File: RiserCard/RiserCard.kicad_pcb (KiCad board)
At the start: 2 copper layers, 150 x 76 mm, 0 parts

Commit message: Mid-work commit. Add README
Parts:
- added U1: 86094327313755ELF, Kicad_Library:DIN41612_C2_2x16_Male_Horizontal_THT, F.Cu at (45.3, 97.0)
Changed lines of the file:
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@@
     (tracks 0)
     (zones 0)
-    (modules 0)
-    (nets 1)
+    (modules 1)
+    (nets 4)
   )
   (page A4)
@@
   )
   (net 0 "")
+  (net 1 +5V)
+  (net 2 +3V3)
+  (net 3 GND)
   (net_class Default "This is the default net class."
     (clearance 0.2)
@@
     (uvia_dia 0.3)
     (uvia_drill 0.1)
+    (add_net +3V3)
+    (add_net +5V)
+    (add_net /EN_ICSP_A)
+    (add_net /EN_ICSP_B)
+    (add_net /EN_JTAG_A)
+    (add_net /EN_JTAG_B)
+    (add_net /EN_PWR_A)
+    (add_net /EN_PWR_B)
+    (add_net /PGEC)
+    (add_net /PGED)
+    (add_net /SPARE_A)
+    (add_net /SPARE_B)
+    (add_net /TARGET_RX)
+    (add_net /TARGET_TX)
+    (add_net /TCK)
+    (add_net /TDI)
+    (add_net /TDO)
+    (add_net /TMS)
+    (add_net /~MCLR)
+    (add_net GND)
+    (add_net "Net-(U1-Pada10)")
+    (add_net "Net-(U1-Pada11)")
+    (add_net "Net-(U1-Pada12)")
+    (add_net "Net-(U1-Pada13)")
+    (add_net "Net-(U1-Pada5)")
+    (add_net "Net-(U1-Pada6)")
+    (add_net "Net-(U1-Pada7)")
+    (add_net "Net-(U1-Pada8)")
+    (add_net "Net-(U1-Pada9)")
+  )
+  (module Kicad_Library:DIN41612_C2_2x16_Male_Horizontal_THT (layer F.Cu)
+    (at 45.3 97.05 90)
+    (descr "DIN41612 connector, type C/2, Horizontal, 3 rows 16 pins wide, https://www.erni-x-press.com/de/downloads/kataloge/englische_kataloge/erni-din41612-iec60603-2-e.pdf")
+    (tags "DIN 41612 IEC 60603 C/2")
+    (fp_text reference U1 (at -5.08 1 90) (layer F.SilkS)
+      (effects (font (size 1 1) (thickness 0.15)))
+    )
+    (fp_text value 86094327313755ELF (at 19.05 7.62 90) (layer F.Fab)
+      (effects (font (size 1 1) (thickness 0.15)))
+    )
+    (fp_text user %R (at 19.05 -2.54 90) (layer F.Fab)
+      (effects (font (size 1 1) (thickness 0.15)))
+    )
+    (fp_text user "Board edge" (at 19.05 -7.3 90) (layer Cmts.User)
+      (effects (font (size 0.7 0.7) (thickness 0.1)))
+    )
+    (fp_line (start 19.05 -5.4) (end 19.05 -6.7) (layer Cmts.User) (width 0.1))
+    (fp_line (start 19.05 -5.4) (end 19.25 -5.9) (layer Cmts.User) (width 0.1))
+    (fp_line (start 18.85 -5.9) (end 19.05 -5.4) (layer Cmts.User) (width 0.1))
+    (fp_line (start -7.9 -5.3) (end 46 -5.3) (layer Dwgs.User) (width 0.08))
+    (fp_line (start 46.5 -13.23) (end -8.39 -13.23) (layer F.CrtYd) (width 0.05))
+    (fp_line (start 46.5 0.5) (end 46.5 -13.23) (layer F.CrtYd) (width 0.05))
+    (fp_line (start 39.38 0.5) (end 46.5 0.5) (layer F.CrtYd) (width 0.05))
+    (fp_line (start 39.38 6.36) (end 39.38 0.5) (layer F.CrtYd) (width 0.05))
+    (fp_line (start -1.27 6.36) (end 39.38 6.36) (layer F.CrtYd) (width 0.05))
+    (fp_line (start -1.27 0.5) (end -1.27 6.36) (layer F.CrtYd) (width 0.05))
+    (fp_line (start -8.39 0.5) (end -1.27 0.5) (layer F.CrtYd) (width 0.05))
+    (fp_line (start -8.39 -13.23) (end -8.39 0.5) (layer F.CrtYd) (width 0.05))
+    (fp_line (start 0.5 -1.9) (end 0 -1.2) (layer F.Fab) (width 0.1))
+    (fp_line (start -0.5 -1.9) (end 0.5 -1.9) (layer F.Fab) (width 0.1))
+    (fp_line (start 0 -1.2) (end -0.5 -1.9) (layer F.Fab) (width 0.1))
+    (fp_line (start -1.695 0.3) (end -1.095 0) (layer F.SilkS) (width 0.12))
+    (fp_line (start -1.695 -0.3) (end -1.695 0.3) (layer F.SilkS) (width 0.12))
+    (fp_line (start -1.095 0) (end -1.695 -0.3) (layer F.SilkS) (width 0.12))
+    (fp_line (start 38.97 -0.74) (end 40.74 -0.74) (layer F.SilkS) (width 0.12))
+    (fp_line (start 36.43 -0.74) (end 37.231 -0.74) (layer F.SilkS) (width 0.12))
+    (fp_line (start 33.89 -0.74) (end 34.691 -0.74) (layer F.SilkS) (width 0.12))
+    (fp_line (start 31.35 -0.74) (end 32.151 -0.74) (layer F.SilkS) (width 0.12))
+    (fp_line (start 28.81 -0.74) (end 29.611 -0.74) (layer F.SilkS) (width 0.12))
+    (fp_line (start 26.27 -0.74) (end 27.071 -0.74) (layer F.SilkS) (width 0.12))
+    (fp_line (start 23.73 -0.74) (end 24.531 -0.74) (layer F.SilkS) (width 0.12))
+    (fp_line (start 21.19 -0.74) (end 21.991 -0.74) (layer F.SilkS) (width 0.12))
+    (fp_line (start 18.65 -0.74) (end 19.451 -0.74) (layer F.SilkS) (width 0.12))
+    (fp_line (start 16.11 -0.74) (end 16.911 -0.74) (layer F.SilkS) (width 0.12))
+    (fp_line (start 13.57 -0.74) (end 14.371 -0.74) (layer F.SilkS) (width 0.12))
+    (fp_line (start 11.03 -0.74) (end 11.831 -0.74) (layer F.SilkS) (width 0.12))
+    (fp_line (start 8.49 -0.74) (end 9.291 -0.74) (layer F.SilkS) (width 0.12))
+    (fp_line (start 5.95 -0.74) (end 6.751 -0.74) (layer F.SilkS) (width 0.12))
+    (fp_line (start 3.41 -0.74) (end 4.211 -0.74) (layer F.SilkS) (width 0.12))
+    (fp_line (start 1.095 -0.74) (end 1.671 -0.74) (layer F.SilkS) (width 0.12))
+    (fp_line (start -2.64 -0.74) (end -1.095 -0.74) (layer F.SilkS) (width 0.12))
+    (fp_line (start 40.74 0.26) (end 40.74 -0.74) (layer F.SilkS) (width 0.12))
+    (fp_line (start 46.26 0.26) (end 40.74 0.26) (layer F.SilkS) (width 0.12))
+    (fp_line (start 46.26 -5.3) (end 46.26 0.26) (layer F.SilkS) (width 0.12))
+    (fp_line (start -2.64 0.26) (end -2.64 -0.74) (layer F.SilkS) (width 0.12))
+    (fp_line (start -8.16 0.26) (end -2.64 0.26) (layer F.SilkS) (width 0.12))
+    (fp_line (start -8.16 -5.3) (end -8.16 0.26) (layer F.SilkS) (width 0.12))
+    (fp_line (start 42.55 -12.74) (end -4.45 -12.74) (layer F.Fab) (width 0.1))
+    (fp_line (start 42.55 -6.74) (end 42.55 -12.74) (layer F.Fab) (width 0.1))
+    (fp_line (start 46 -6.74) (end 42.55 -6.74) (layer F.Fab) (width 0.1))
+    (fp_line (start 46 0) (end 46 -6.74) (layer F.Fab) (width 0.1))
+    (fp_line (start 41 0) (end 46 0) (layer F.Fab) (width 0.1))
+    (fp_line (start 41 -1) (end 41 0) (layer F.Fab) (width 0.1))
+    (fp_line (start -2.9 -1) (end 41 -1) (layer F.Fab) (width 0.1))
+    (fp_line (start -2.9 0) (end -2.9 -1) (layer F.Fab) (width 0.1))
+    (fp_line (start -7.9 0) (end -2.9 0) (layer F.Fab) (width 0.1))
+    (fp_line (start -7.9 -6.74) (end -7.9 0) (layer F.Fab) (width 0.1))
+    (fp_line (start -4.45 -6.74) (end -7.9 -6.74) (layer F.Fab) (width 0.1))
+    (fp_line (start -4.45 -12.74) (end -4.45 -6.74) (layer F.Fab) (width 0.1))
+    (pad "" np_thru_hole circle (at -5.08 -2.54 90) (size 2.85 2.85) (drill 2.85) (layers *.Cu *.Mask))
+    (pad "" np_thru_hole circle (at 43.18 -2.54 90) (size 2.85 2.85) (drill 2.85) (layers *.Cu *.Mask))
+    (pad a1 thru_hole roundrect (at 0 0 90) (size 1.55 1.55) (drill 1) (layers *.Cu *.Mask) (roundrect_rratio 0.16129))
+    (pad a2 thru_hole circle (at 2.54 0 90) (size 1.55 1.55) (drill 1) (layers *.Cu *.Mask))
+    (pad a3 thru_hole circle (at 5.08 0 90) (size 1.55 1.55) (drill 1) (layers *.Cu *.Mask))
+    (pad a4 thru_hole circle (at 7.62 0 90) (size 1.55 1.55) (drill 1) (layers *.Cu *.Mask))
+    (pad a5 thru_hole circle (at 10.16 0 90) (size 1.55 1.55) (drill 1) (layers *.Cu *.Mask))
+    (pad a6 thru_hole circle (at 12.7 0 90) (size 1.55 1.55) (drill 1) (layers *.Cu *.Mask))
+    (pad a7 thru_hole circle (at 15.24 0 90) (size 1.55 1.55) (drill 1) (layers *.Cu *.Mask))
+    (pad a8 thru_hole circle (at 17.78 0 90) (size 1.55 1.55) (drill 1) (layers *.Cu *.Mask))
+    (pad a9 thru_hole circle (at 20.32 0 90) (size 1.55 1.55) (drill 1) (layers *.Cu *.Mask))
+    (pad a10 thru_hole circle (at 22.86 0 90) (size 1.55 1.55) (drill 1) (layers *.Cu *.Mask))
+    (pad a11 thru_hole circle (at 25.4 0 90) (size 1.55 1.55) (drill 1) (layers *.Cu *.Mask))
+    (pad a12 thru_hole circle (at 27.94 0 90) (size 1.55 1.55) (drill 1) (layers *.Cu *.Mask))
+    (pad a13 thru_hole circle (at 30.48 0 90) (size 1.55 1.55) (drill 1) (layers *.Cu *.Mask))
+    (pad a14 thru_hole circle (at 33.02 0 90) (size 1.55 1.55) (drill 1) (layers *.Cu *.Mask)
+      (net 1 +5V))
+    (pad a15 thru_hole circle (at 35.56 0 90) (size 1.55 1.55) (drill 1) (layers *.Cu *.Mask)
+      (net 2 +3V3))
+    (pad a16 thru_hole circle (at 38.1 0 90) (size 1.55 1.55) (drill 1) (layers *.Cu *.Mask)
+      (net 3 GND))
+    (pad c1 thru_hole circle (at 0 5.08 90) (size 1.55 1.55) (drill 1) (layers *.Cu *.Mask))
+    (pad c2 thru_hole circle (at 2.54 5.08 90) (size 1.55 1.55) (drill 1) (layers *.Cu *.Mask))
+    (pad c3 thru_hole circle (at 5.08 5.08 90) (size 1.55 1.55) (drill 1) (layers *.Cu *.Mask))
+    (pad c4 thru_hole circle (at 7.62 5.08 90) (size 1.55 1.55) (drill 1) (layers *.Cu *.Mask))
+    (pad c5 thru_hole circle (at 10.16 5.08 90) (size 1.55 1.55) (drill 1) (layers *.Cu *.Mask))
+    (pad c6 thru_hole circle (at 12.7 5.08 90) (size 1.55 1.55) (drill 1) (layers *.Cu *.Mask))
+    (pad c7 thru_hole circle (at 15.24 5.08 90) (size 1.55 1.55) (drill 1) (layers *.Cu *.Mask))
+    (pad c8 thru_hole circle (at 17.78 5.08 90) (size 1.55 1.55) (drill 1) (layers *.Cu *.Mask))
+    (pad c9 thru_hole circle (at 20.32 5.08 90) (size 1.55 1.55) (drill 1) (layers *.Cu *.Mask))
+    (pad c10 thru_hole circle (at 22.86 5.08 90) (size 1.55 1.55) (drill 1) (layers *.Cu *.Mask))
+    (pad c11 thru_hole circle (at 25.4 5.08 90) (size 1.55 1.55) (drill 1) (layers *.Cu *.Mask))
+    (pad c12 thru_hole circle (at 27.94 5.08 90) (size 1.55 1.55) (drill 1) (layers *.Cu *.Mask))
+    (pad c13 thru_hole circle (at 30.48 5.08 90) (size 1.55 1.55) (drill 1) (layers *.Cu *.Mask))
+    (pad c14 thru_hole circle (at 33.02 5.08 90) (size 1.55 1.55) (drill 1) (layers *.Cu *.Mask)
+      (net 1 +5V))
+    (pad c15 thru_hole circle (at 35.56 5.08 90) (size 1.55 1.55) (drill 1) (layers *.Cu *.Mask)
+      (net 2 +3V3))
+    (pad c16 thru_hole circle (at 38.1 5.08 90) (size 1.55 1.55) (drill 1) (layers *.Cu *.Mask)
+      (net 3 GND))
+    (model ${KICUSTOM3DMOD}/86094327313755ELF.stp
+      (offset (xyz 43.45 15 10.8))
+      (scale (xyz 1 1 1))
+      (rotate (xyz 0 0 180))
+    )
   )
   (gr_line (start 190 40) (end 40 40) (layer Edge.Cuts) (width 0.05))

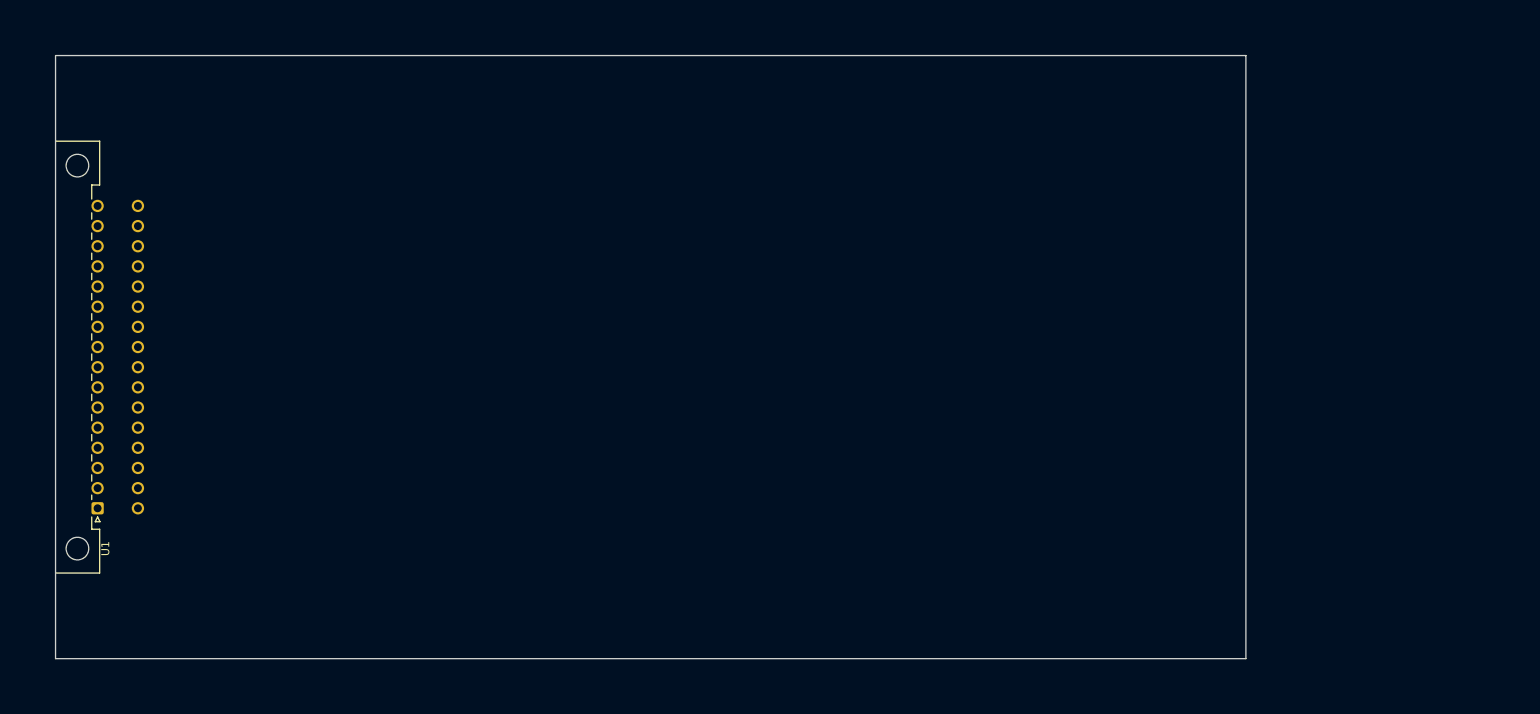
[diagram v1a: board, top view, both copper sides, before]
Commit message: mid-work commit, preparing the riser card
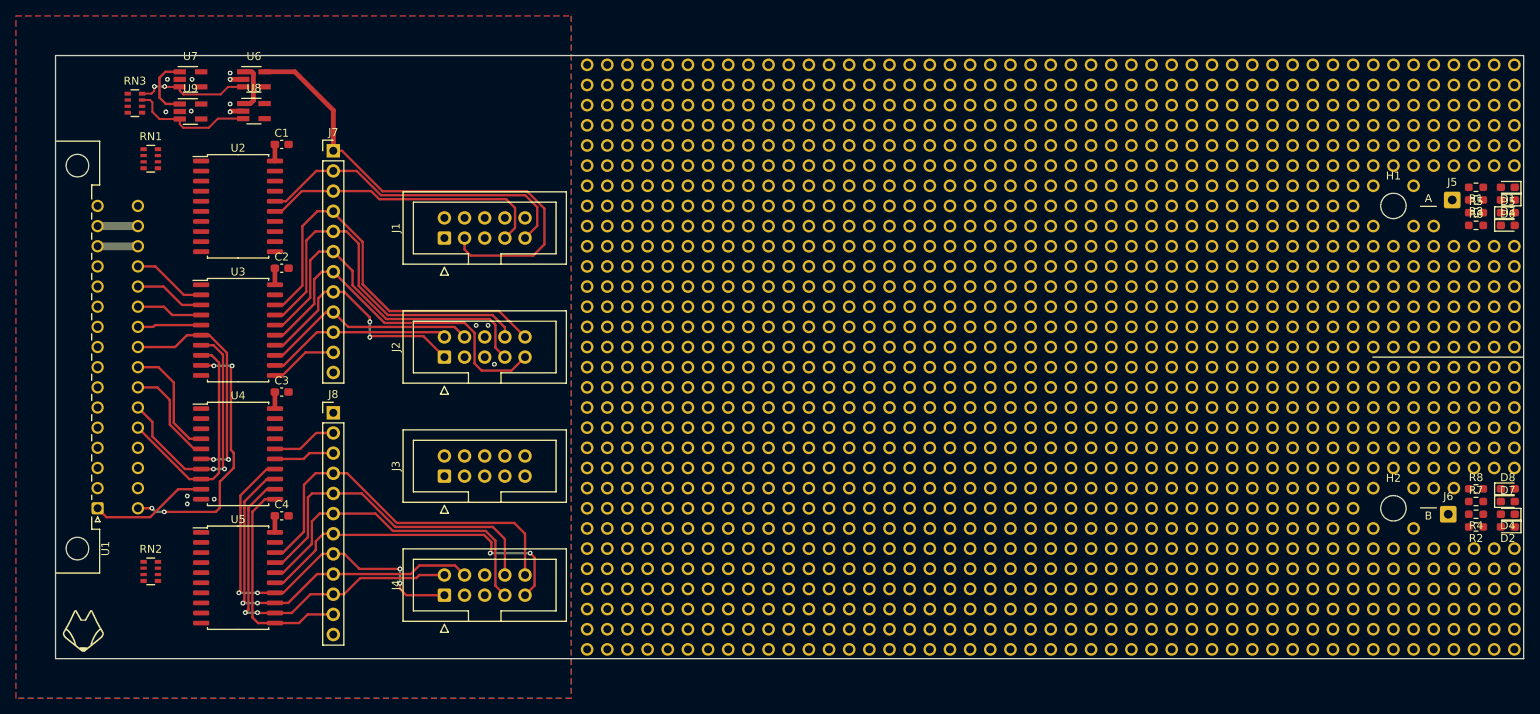
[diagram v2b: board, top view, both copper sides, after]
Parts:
- added C1: 100nF, Capacitor_SMD:C_0603_1608Metric_Pad1.08x0.95mm_HandSolder, F.Cu at (68.5, 51.2)
- added C2: 100nF, Capacitor_SMD:C_0603_1608Metric_Pad1.08x0.95mm_HandSolder, F.Cu at (68.5, 66.8)
- added C3: 100nF, Capacitor_SMD:C_0603_1608Metric_Pad1.08x0.95mm_HandSolder, F.Cu at (68.5, 82.4)
- added C4: 100nF, Capacitor_SMD:C_0603_1608Metric_Pad1.08x0.95mm_HandSolder, F.Cu at (68.5, 98.0)
- added D1: LED, LED_SMD:LED_0603_1608Metric_Pad1.05x0.95mm_HandSolder, F.Cu at (223.0, 56.6)
- added D2: LED, LED_SMD:LED_0603_1608Metric_Pad1.05x0.95mm_HandSolder, F.Cu at (223.0, 99.4)
- added D3: LED, LED_SMD:LED_0603_1608Metric_Pad1.05x0.95mm_HandSolder, F.Cu at (223.0, 58.2)
- added D4: LED, LED_SMD:LED_0603_1608Metric_Pad1.05x0.95mm_HandSolder, F.Cu at (223.0, 97.8)
- added D5: LED, LED_SMD:LED_0603_1608Metric_Pad1.05x0.95mm_HandSolder, F.Cu at (223.0, 59.8)
- added D6: LED, LED_SMD:LED_0603_1608Metric_Pad1.05x0.95mm_HandSolder, F.Cu at (223.0, 61.4)
- added D7: LED, LED_SMD:LED_0603_1608Metric_Pad1.05x0.95mm_HandSolder, F.Cu at (223.0, 96.2)
- added D8: LED, LED_SMD:LED_0603_1608Metric_Pad1.05x0.95mm_HandSolder, F.Cu at (223.0, 94.6)
- added H1: MountingHole, MountingHole:MountingHole_3.2mm_M3_DIN965, F.Cu at (208.6, 59.0)
- added H2: MountingHole, MountingHole:MountingHole_3.2mm_M3_DIN965, F.Cu at (208.6, 97.0)
- added H3: MountingHole_Pad, Kicad_Library:ThroughHoleSingleSide_1mm_1.6mm, B.Cu at (208.6, 76.7)
- added H3: MountingHole_Pad, Kicad_Library:ThroughHoleSingleSide_1mm_1.6mm, B.Cu at (117.2, 114.8)
- added H3: MountingHole_Pad, Kicad_Library:ThroughHoleSingleSide_1mm_1.6mm, B.Cu at (107.0, 109.8)
- added H3: MountingHole_Pad, Kicad_Library:ThroughHoleSingleSide_1mm_1.6mm, B.Cu at (183.2, 61.5)
- added H3: MountingHole_Pad, Kicad_Library:ThroughHoleSingleSide_1mm_1.6mm, B.Cu at (185.7, 61.5)
- added H3: MountingHole_Pad, Kicad_Library:ThroughHoleSingleSide_1mm_1.6mm, B.Cu at (188.3, 61.5)
- added H3: MountingHole_Pad, Kicad_Library:ThroughHoleSingleSide_1mm_1.6mm, B.Cu at (190.8, 61.5)
- added H3: MountingHole_Pad, Kicad_Library:ThroughHoleSingleSide_1mm_1.6mm, B.Cu at (193.3, 61.5)
- added H3: MountingHole_Pad, Kicad_Library:ThroughHoleSingleSide_1mm_1.6mm, B.Cu at (195.9, 61.5)
- added H3: MountingHole_Pad, Kicad_Library:ThroughHoleSingleSide_1mm_1.6mm, B.Cu at (198.4, 61.5)
- added H3: MountingHole_Pad, Kicad_Library:ThroughHoleSingleSide_1mm_1.6mm, B.Cu at (201.0, 61.5)
- added H3: MountingHole_Pad, Kicad_Library:ThroughHoleSingleSide_1mm_1.6mm, B.Cu at (203.5, 61.5)
- added H3: MountingHole_Pad, Kicad_Library:ThroughHoleSingleSide_1mm_1.6mm, B.Cu at (206.1, 61.5)
- added H3: MountingHole_Pad, Kicad_Library:ThroughHoleSingleSide_1mm_1.6mm, B.Cu at (109.5, 109.8)
- added H3: MountingHole_Pad, Kicad_Library:ThroughHoleSingleSide_1mm_1.6mm, B.Cu at (211.1, 61.5)
- added H3: MountingHole_Pad, Kicad_Library:ThroughHoleSingleSide_1mm_1.6mm, B.Cu at (213.7, 61.5)
- added H3: MountingHole_Pad, Kicad_Library:ThroughHoleSingleSide_1mm_1.6mm, B.Cu at (107.0, 59.0)
- added H3: MountingHole_Pad, Kicad_Library:ThroughHoleSingleSide_1mm_1.6mm, B.Cu at (109.5, 59.0)
- added H3: MountingHole_Pad, Kicad_Library:ThroughHoleSingleSide_1mm_1.6mm, B.Cu at (112.1, 59.0)
- added H3: MountingHole_Pad, Kicad_Library:ThroughHoleSingleSide_1mm_1.6mm, B.Cu at (114.6, 59.0)
- added H3: MountingHole_Pad, Kicad_Library:ThroughHoleSingleSide_1mm_1.6mm, B.Cu at (117.2, 59.0)
- added H3: MountingHole_Pad, Kicad_Library:ThroughHoleSingleSide_1mm_1.6mm, B.Cu at (119.7, 59.0)
- added H3: MountingHole_Pad, Kicad_Library:ThroughHoleSingleSide_1mm_1.6mm, B.Cu at (122.2, 59.0)
- added H3: MountingHole_Pad, Kicad_Library:ThroughHoleSingleSide_1mm_1.6mm, B.Cu at (124.8, 59.0)
- added H3: MountingHole_Pad, Kicad_Library:ThroughHoleSingleSide_1mm_1.6mm, B.Cu at (112.1, 109.8)
- added H3: MountingHole_Pad, Kicad_Library:ThroughHoleSingleSide_1mm_1.6mm, B.Cu at (127.3, 59.0)
- added H3: MountingHole_Pad, Kicad_Library:ThroughHoleSingleSide_1mm_1.6mm, B.Cu at (129.8, 59.0)
- added H3: MountingHole_Pad, Kicad_Library:ThroughHoleSingleSide_1mm_1.6mm, B.Cu at (132.4, 59.0)
- added H3: MountingHole_Pad, Kicad_Library:ThroughHoleSingleSide_1mm_1.6mm, B.Cu at (134.9, 59.0)
- added H3: MountingHole_Pad, Kicad_Library:ThroughHoleSingleSide_1mm_1.6mm, B.Cu at (137.5, 59.0)
- added H3: MountingHole_Pad, Kicad_Library:ThroughHoleSingleSide_1mm_1.6mm, B.Cu at (140.0, 59.0)
- added H3: MountingHole_Pad, Kicad_Library:ThroughHoleSingleSide_1mm_1.6mm, B.Cu at (142.6, 59.0)
- added H3: MountingHole_Pad, Kicad_Library:ThroughHoleSingleSide_1mm_1.6mm, B.Cu at (145.1, 59.0)
- added H3: MountingHole_Pad, Kicad_Library:ThroughHoleSingleSide_1mm_1.6mm, B.Cu at (147.6, 59.0)
- added H3: MountingHole_Pad, Kicad_Library:ThroughHoleSingleSide_1mm_1.6mm, B.Cu at (150.2, 59.0)
- added H3: MountingHole_Pad, Kicad_Library:ThroughHoleSingleSide_1mm_1.6mm, B.Cu at (114.6, 109.8)
- added H3: MountingHole_Pad, Kicad_Library:ThroughHoleSingleSide_1mm_1.6mm, B.Cu at (152.7, 59.0)
- added H3: MountingHole_Pad, Kicad_Library:ThroughHoleSingleSide_1mm_1.6mm, B.Cu at (155.2, 59.0)
- added H3: MountingHole_Pad, Kicad_Library:ThroughHoleSingleSide_1mm_1.6mm, B.Cu at (157.8, 59.0)
- added H3: MountingHole_Pad, Kicad_Library:ThroughHoleSingleSide_1mm_1.6mm, B.Cu at (160.3, 59.0)
- added H3: MountingHole_Pad, Kicad_Library:ThroughHoleSingleSide_1mm_1.6mm, B.Cu at (162.9, 59.0)
- added H3: MountingHole_Pad, Kicad_Library:ThroughHoleSingleSide_1mm_1.6mm, B.Cu at (165.4, 59.0)
- added H3: MountingHole_Pad, Kicad_Library:ThroughHoleSingleSide_1mm_1.6mm, B.Cu at (167.9, 59.0)
- added H3: MountingHole_Pad, Kicad_Library:ThroughHoleSingleSide_1mm_1.6mm, B.Cu at (170.5, 59.0)
- added H3: MountingHole_Pad, Kicad_Library:ThroughHoleSingleSide_1mm_1.6mm, B.Cu at (173.0, 59.0)
- added H3: MountingHole_Pad, Kicad_Library:ThroughHoleSingleSide_1mm_1.6mm, B.Cu at (175.6, 59.0)
- added H3: MountingHole_Pad, Kicad_Library:ThroughHoleSingleSide_1mm_1.6mm, B.Cu at (117.2, 109.8)
- added H3: MountingHole_Pad, Kicad_Library:ThroughHoleSingleSide_1mm_1.6mm, B.Cu at (178.1, 59.0)
- added H3: MountingHole_Pad, Kicad_Library:ThroughHoleSingleSide_1mm_1.6mm, B.Cu at (180.7, 59.0)
- added H3: MountingHole_Pad, Kicad_Library:ThroughHoleSingleSide_1mm_1.6mm, B.Cu at (183.2, 59.0)
- added H3: MountingHole_Pad, Kicad_Library:ThroughHoleSingleSide_1mm_1.6mm, B.Cu at (185.7, 59.0)
- added H3: MountingHole_Pad, Kicad_Library:ThroughHoleSingleSide_1mm_1.6mm, B.Cu at (188.3, 59.0)
- added H3: MountingHole_Pad, Kicad_Library:ThroughHoleSingleSide_1mm_1.6mm, B.Cu at (190.8, 59.0)
- added H3: MountingHole_Pad, Kicad_Library:ThroughHoleSingleSide_1mm_1.6mm, B.Cu at (193.3, 59.0)
- added H3: MountingHole_Pad, Kicad_Library:ThroughHoleSingleSide_1mm_1.6mm, B.Cu at (195.9, 59.0)
- added H3: MountingHole_Pad, Kicad_Library:ThroughHoleSingleSide_1mm_1.6mm, B.Cu at (198.4, 59.0)
- added H3: MountingHole_Pad, Kicad_Library:ThroughHoleSingleSide_1mm_1.6mm, B.Cu at (201.0, 59.0)
- added H3: MountingHole_Pad, Kicad_Library:ThroughHoleSingleSide_1mm_1.6mm, B.Cu at (119.7, 109.8)
- added H3: MountingHole_Pad, Kicad_Library:ThroughHoleSingleSide_1mm_1.6mm, B.Cu at (203.5, 59.0)
- added H3: MountingHole_Pad, Kicad_Library:ThroughHoleSingleSide_1mm_1.6mm, B.Cu at (107.0, 56.4)
- added H3: MountingHole_Pad, Kicad_Library:ThroughHoleSingleSide_1mm_1.6mm, B.Cu at (109.5, 56.4)
- added H3: MountingHole_Pad, Kicad_Library:ThroughHoleSingleSide_1mm_1.6mm, B.Cu at (112.1, 56.4)
- added H3: MountingHole_Pad, Kicad_Library:ThroughHoleSingleSide_1mm_1.6mm, B.Cu at (114.6, 56.4)
- added H3: MountingHole_Pad, Kicad_Library:ThroughHoleSingleSide_1mm_1.6mm, B.Cu at (117.2, 56.4)
- added H3: MountingHole_Pad, Kicad_Library:ThroughHoleSingleSide_1mm_1.6mm, B.Cu at (119.7, 56.4)
- added H3: MountingHole_Pad, Kicad_Library:ThroughHoleSingleSide_1mm_1.6mm, B.Cu at (122.2, 56.4)
- added H3: MountingHole_Pad, Kicad_Library:ThroughHoleSingleSide_1mm_1.6mm, B.Cu at (124.8, 56.4)
- added H3: MountingHole_Pad, Kicad_Library:ThroughHoleSingleSide_1mm_1.6mm, B.Cu at (127.3, 56.4)
- added H3: MountingHole_Pad, Kicad_Library:ThroughHoleSingleSide_1mm_1.6mm, B.Cu at (122.2, 109.8)
- added H3: MountingHole_Pad, Kicad_Library:ThroughHoleSingleSide_1mm_1.6mm, B.Cu at (129.8, 56.4)
- added H3: MountingHole_Pad, Kicad_Library:ThroughHoleSingleSide_1mm_1.6mm, B.Cu at (132.4, 56.4)
- added H3: MountingHole_Pad, Kicad_Library:ThroughHoleSingleSide_1mm_1.6mm, B.Cu at (134.9, 56.4)
- added H3: MountingHole_Pad, Kicad_Library:ThroughHoleSingleSide_1mm_1.6mm, B.Cu at (137.5, 56.4)
- added H3: MountingHole_Pad, Kicad_Library:ThroughHoleSingleSide_1mm_1.6mm, B.Cu at (140.0, 56.4)
- added H3: MountingHole_Pad, Kicad_Library:ThroughHoleSingleSide_1mm_1.6mm, B.Cu at (142.6, 56.4)
- added H3: MountingHole_Pad, Kicad_Library:ThroughHoleSingleSide_1mm_1.6mm, B.Cu at (145.1, 56.4)
- added H3: MountingHole_Pad, Kicad_Library:ThroughHoleSingleSide_1mm_1.6mm, B.Cu at (147.6, 56.4)
- added H3: MountingHole_Pad, Kicad_Library:ThroughHoleSingleSide_1mm_1.6mm, B.Cu at (150.2, 56.4)
- added H3: MountingHole_Pad, Kicad_Library:ThroughHoleSingleSide_1mm_1.6mm, B.Cu at (152.7, 56.4)
- added H3: MountingHole_Pad, Kicad_Library:ThroughHoleSingleSide_1mm_1.6mm, B.Cu at (124.8, 109.8)
- added H3: MountingHole_Pad, Kicad_Library:ThroughHoleSingleSide_1mm_1.6mm, B.Cu at (155.2, 56.4)
- added H3: MountingHole_Pad, Kicad_Library:ThroughHoleSingleSide_1mm_1.6mm, B.Cu at (157.8, 56.4)
- added H3: MountingHole_Pad, Kicad_Library:ThroughHoleSingleSide_1mm_1.6mm, B.Cu at (160.3, 56.4)
- added H3: MountingHole_Pad, Kicad_Library:ThroughHoleSingleSide_1mm_1.6mm, B.Cu at (162.9, 56.4)
- added H3: MountingHole_Pad, Kicad_Library:ThroughHoleSingleSide_1mm_1.6mm, B.Cu at (165.4, 56.4)
- added H3: MountingHole_Pad, Kicad_Library:ThroughHoleSingleSide_1mm_1.6mm, B.Cu at (167.9, 56.4)
- added H3: MountingHole_Pad, Kicad_Library:ThroughHoleSingleSide_1mm_1.6mm, B.Cu at (170.5, 56.4)
- added H3: MountingHole_Pad, Kicad_Library:ThroughHoleSingleSide_1mm_1.6mm, B.Cu at (173.0, 56.4)
- added H3: MountingHole_Pad, Kicad_Library:ThroughHoleSingleSide_1mm_1.6mm, B.Cu at (175.6, 56.4)
- added H3: MountingHole_Pad, Kicad_Library:ThroughHoleSingleSide_1mm_1.6mm, B.Cu at (178.1, 56.4)
- added H3: MountingHole_Pad, Kicad_Library:ThroughHoleSingleSide_1mm_1.6mm, B.Cu at (127.3, 109.8)
- added H3: MountingHole_Pad, Kicad_Library:ThroughHoleSingleSide_1mm_1.6mm, B.Cu at (180.7, 56.4)
- added H3: MountingHole_Pad, Kicad_Library:ThroughHoleSingleSide_1mm_1.6mm, B.Cu at (183.2, 56.4)
- added H3: MountingHole_Pad, Kicad_Library:ThroughHoleSingleSide_1mm_1.6mm, B.Cu at (185.7, 56.4)
- added H3: MountingHole_Pad, Kicad_Library:ThroughHoleSingleSide_1mm_1.6mm, B.Cu at (188.3, 56.4)
- added H3: MountingHole_Pad, Kicad_Library:ThroughHoleSingleSide_1mm_1.6mm, B.Cu at (190.8, 56.4)
- added H3: MountingHole_Pad, Kicad_Library:ThroughHoleSingleSide_1mm_1.6mm, B.Cu at (193.3, 56.4)
- added H3: MountingHole_Pad, Kicad_Library:ThroughHoleSingleSide_1mm_1.6mm, B.Cu at (195.9, 56.4)
- added H3: MountingHole_Pad, Kicad_Library:ThroughHoleSingleSide_1mm_1.6mm, B.Cu at (198.4, 56.4)
- added H3: MountingHole_Pad, Kicad_Library:ThroughHoleSingleSide_1mm_1.6mm, B.Cu at (201.0, 56.4)
- added H3: MountingHole_Pad, Kicad_Library:ThroughHoleSingleSide_1mm_1.6mm, B.Cu at (203.5, 56.4)
- added H3: MountingHole_Pad, Kicad_Library:ThroughHoleSingleSide_1mm_1.6mm, B.Cu at (129.8, 109.8)
- added H3: MountingHole_Pad, Kicad_Library:ThroughHoleSingleSide_1mm_1.6mm, B.Cu at (206.1, 56.4)
- added H3: MountingHole_Pad, Kicad_Library:ThroughHoleSingleSide_1mm_1.6mm, B.Cu at (211.1, 56.4)
- added H3: MountingHole_Pad, Kicad_Library:ThroughHoleSingleSide_1mm_1.6mm, B.Cu at (107.0, 53.9)
- added H3: MountingHole_Pad, Kicad_Library:ThroughHoleSingleSide_1mm_1.6mm, B.Cu at (109.5, 53.9)
- added H3: MountingHole_Pad, Kicad_Library:ThroughHoleSingleSide_1mm_1.6mm, B.Cu at (112.1, 53.9)
- added H3: MountingHole_Pad, Kicad_Library:ThroughHoleSingleSide_1mm_1.6mm, B.Cu at (114.6, 53.9)
- added H3: MountingHole_Pad, Kicad_Library:ThroughHoleSingleSide_1mm_1.6mm, B.Cu at (117.2, 53.9)
- added H3: MountingHole_Pad, Kicad_Library:ThroughHoleSingleSide_1mm_1.6mm, B.Cu at (119.7, 53.9)
- added H3: MountingHole_Pad, Kicad_Library:ThroughHoleSingleSide_1mm_1.6mm, B.Cu at (122.2, 53.9)
- added H3: MountingHole_Pad, Kicad_Library:ThroughHoleSingleSide_1mm_1.6mm, B.Cu at (124.8, 53.9)
- added H3: MountingHole_Pad, Kicad_Library:ThroughHoleSingleSide_1mm_1.6mm, B.Cu at (119.7, 114.8)
- added H3: MountingHole_Pad, Kicad_Library:ThroughHoleSingleSide_1mm_1.6mm, B.Cu at (132.4, 109.8)
- added H3: MountingHole_Pad, Kicad_Library:ThroughHoleSingleSide_1mm_1.6mm, B.Cu at (127.3, 53.9)
- added H3: MountingHole_Pad, Kicad_Library:ThroughHoleSingleSide_1mm_1.6mm, B.Cu at (129.8, 53.9)
- added H3: MountingHole_Pad, Kicad_Library:ThroughHoleSingleSide_1mm_1.6mm, B.Cu at (132.4, 53.9)
- added H3: MountingHole_Pad, Kicad_Library:ThroughHoleSingleSide_1mm_1.6mm, B.Cu at (134.9, 53.9)
- added H3: MountingHole_Pad, Kicad_Library:ThroughHoleSingleSide_1mm_1.6mm, B.Cu at (137.5, 53.9)
- added H3: MountingHole_Pad, Kicad_Library:ThroughHoleSingleSide_1mm_1.6mm, B.Cu at (140.0, 53.9)
- added H3: MountingHole_Pad, Kicad_Library:ThroughHoleSingleSide_1mm_1.6mm, B.Cu at (142.6, 53.9)
- added H3: MountingHole_Pad, Kicad_Library:ThroughHoleSingleSide_1mm_1.6mm, B.Cu at (145.1, 53.9)
- added H3: MountingHole_Pad, Kicad_Library:ThroughHoleSingleSide_1mm_1.6mm, B.Cu at (147.6, 53.9)
- added H3: MountingHole_Pad, Kicad_Library:ThroughHoleSingleSide_1mm_1.6mm, B.Cu at (150.2, 53.9)
- added H3: MountingHole_Pad, Kicad_Library:ThroughHoleSingleSide_1mm_1.6mm, B.Cu at (134.9, 109.8)
- added H3: MountingHole_Pad, Kicad_Library:ThroughHoleSingleSide_1mm_1.6mm, B.Cu at (152.7, 53.9)
- added H3: MountingHole_Pad, Kicad_Library:ThroughHoleSingleSide_1mm_1.6mm, B.Cu at (155.2, 53.9)
- added H3: MountingHole_Pad, Kicad_Library:ThroughHoleSingleSide_1mm_1.6mm, B.Cu at (157.8, 53.9)
- added H3: MountingHole_Pad, Kicad_Library:ThroughHoleSingleSide_1mm_1.6mm, B.Cu at (160.3, 53.9)
- added H3: MountingHole_Pad, Kicad_Library:ThroughHoleSingleSide_1mm_1.6mm, B.Cu at (162.9, 53.9)
- added H3: MountingHole_Pad, Kicad_Library:ThroughHoleSingleSide_1mm_1.6mm, B.Cu at (165.4, 53.9)
- added H3: MountingHole_Pad, Kicad_Library:ThroughHoleSingleSide_1mm_1.6mm, B.Cu at (167.9, 53.9)
- added H3: MountingHole_Pad, Kicad_Library:ThroughHoleSingleSide_1mm_1.6mm, B.Cu at (170.5, 53.9)
- added H3: MountingHole_Pad, Kicad_Library:ThroughHoleSingleSide_1mm_1.6mm, B.Cu at (173.0, 53.9)
- added H3: MountingHole_Pad, Kicad_Library:ThroughHoleSingleSide_1mm_1.6mm, B.Cu at (175.6, 53.9)
- added H3: MountingHole_Pad, Kicad_Library:ThroughHoleSingleSide_1mm_1.6mm, B.Cu at (137.5, 109.8)
- added H3: MountingHole_Pad, Kicad_Library:ThroughHoleSingleSide_1mm_1.6mm, B.Cu at (178.1, 53.9)
- added H3: MountingHole_Pad, Kicad_Library:ThroughHoleSingleSide_1mm_1.6mm, B.Cu at (180.7, 53.9)
- added H3: MountingHole_Pad, Kicad_Library:ThroughHoleSingleSide_1mm_1.6mm, B.Cu at (183.2, 53.9)
- added H3: MountingHole_Pad, Kicad_Library:ThroughHoleSingleSide_1mm_1.6mm, B.Cu at (185.7, 53.9)
- added H3: MountingHole_Pad, Kicad_Library:ThroughHoleSingleSide_1mm_1.6mm, B.Cu at (188.3, 53.9)
- added H3: MountingHole_Pad, Kicad_Library:ThroughHoleSingleSide_1mm_1.6mm, B.Cu at (190.8, 53.9)
- added H3: MountingHole_Pad, Kicad_Library:ThroughHoleSingleSide_1mm_1.6mm, B.Cu at (193.3, 53.9)
- added H3: MountingHole_Pad, Kicad_Library:ThroughHoleSingleSide_1mm_1.6mm, B.Cu at (195.9, 53.9)
- added H3: MountingHole_Pad, Kicad_Library:ThroughHoleSingleSide_1mm_1.6mm, B.Cu at (198.4, 53.9)
- added H3: MountingHole_Pad, Kicad_Library:ThroughHoleSingleSide_1mm_1.6mm, B.Cu at (201.0, 53.9)
- added H3: MountingHole_Pad, Kicad_Library:ThroughHoleSingleSide_1mm_1.6mm, B.Cu at (140.0, 109.8)
- added H3: MountingHole_Pad, Kicad_Library:ThroughHoleSingleSide_1mm_1.6mm, B.Cu at (203.5, 53.9)
- added H3: MountingHole_Pad, Kicad_Library:ThroughHoleSingleSide_1mm_1.6mm, B.Cu at (206.1, 53.9)
- added H3: MountingHole_Pad, Kicad_Library:ThroughHoleSingleSide_1mm_1.6mm, B.Cu at (208.6, 53.9)
- added H3: MountingHole_Pad, Kicad_Library:ThroughHoleSingleSide_1mm_1.6mm, B.Cu at (211.1, 53.9)
- added H3: MountingHole_Pad, Kicad_Library:ThroughHoleSingleSide_1mm_1.6mm, B.Cu at (213.7, 53.9)
- added H3: MountingHole_Pad, Kicad_Library:ThroughHoleSingleSide_1mm_1.6mm, B.Cu at (216.2, 53.9)
- added H3: MountingHole_Pad, Kicad_Library:ThroughHoleSingleSide_1mm_1.6mm, B.Cu at (218.8, 53.9)
- added H3: MountingHole_Pad, Kicad_Library:ThroughHoleSingleSide_1mm_1.6mm, B.Cu at (221.3, 53.9)
- added H3: MountingHole_Pad, Kicad_Library:ThroughHoleSingleSide_1mm_1.6mm, B.Cu at (223.8, 53.9)
- added H3: MountingHole_Pad, Kicad_Library:ThroughHoleSingleSide_1mm_1.6mm, B.Cu at (107.0, 51.3)
- added H3: MountingHole_Pad, Kicad_Library:ThroughHoleSingleSide_1mm_1.6mm, B.Cu at (142.6, 109.8)
- added H3: MountingHole_Pad, Kicad_Library:ThroughHoleSingleSide_1mm_1.6mm, B.Cu at (109.5, 51.3)
- added H3: MountingHole_Pad, Kicad_Library:ThroughHoleSingleSide_1mm_1.6mm, B.Cu at (112.1, 51.3)
- added H3: MountingHole_Pad, Kicad_Library:ThroughHoleSingleSide_1mm_1.6mm, B.Cu at (114.6, 51.3)
- added H3: MountingHole_Pad, Kicad_Library:ThroughHoleSingleSide_1mm_1.6mm, B.Cu at (117.2, 51.3)
- added H3: MountingHole_Pad, Kicad_Library:ThroughHoleSingleSide_1mm_1.6mm, B.Cu at (119.7, 51.3)
- added H3: MountingHole_Pad, Kicad_Library:ThroughHoleSingleSide_1mm_1.6mm, B.Cu at (122.2, 51.3)
- added H3: MountingHole_Pad, Kicad_Library:ThroughHoleSingleSide_1mm_1.6mm, B.Cu at (124.8, 51.3)
- added H3: MountingHole_Pad, Kicad_Library:ThroughHoleSingleSide_1mm_1.6mm, B.Cu at (127.3, 51.3)
- added H3: MountingHole_Pad, Kicad_Library:ThroughHoleSingleSide_1mm_1.6mm, B.Cu at (129.8, 51.3)
- added H3: MountingHole_Pad, Kicad_Library:ThroughHoleSingleSide_1mm_1.6mm, B.Cu at (132.4, 51.3)
- added H3: MountingHole_Pad, Kicad_Library:ThroughHoleSingleSide_1mm_1.6mm, B.Cu at (145.1, 109.8)
- added H3: MountingHole_Pad, Kicad_Library:ThroughHoleSingleSide_1mm_1.6mm, B.Cu at (134.9, 51.3)
- added H3: MountingHole_Pad, Kicad_Library:ThroughHoleSingleSide_1mm_1.6mm, B.Cu at (137.5, 51.3)
- added H3: MountingHole_Pad, Kicad_Library:ThroughHoleSingleSide_1mm_1.6mm, B.Cu at (140.0, 51.3)
- added H3: MountingHole_Pad, Kicad_Library:ThroughHoleSingleSide_1mm_1.6mm, B.Cu at (142.6, 51.3)
- added H3: MountingHole_Pad, Kicad_Library:ThroughHoleSingleSide_1mm_1.6mm, B.Cu at (145.1, 51.3)
- added H3: MountingHole_Pad, Kicad_Library:ThroughHoleSingleSide_1mm_1.6mm, B.Cu at (147.6, 51.3)
- added H3: MountingHole_Pad, Kicad_Library:ThroughHoleSingleSide_1mm_1.6mm, B.Cu at (150.2, 51.3)
- added H3: MountingHole_Pad, Kicad_Library:ThroughHoleSingleSide_1mm_1.6mm, B.Cu at (152.7, 51.3)
- added H3: MountingHole_Pad, Kicad_Library:ThroughHoleSingleSide_1mm_1.6mm, B.Cu at (155.2, 51.3)
- added H3: MountingHole_Pad, Kicad_Library:ThroughHoleSingleSide_1mm_1.6mm, B.Cu at (157.8, 51.3)
- added H3: MountingHole_Pad, Kicad_Library:ThroughHoleSingleSide_1mm_1.6mm, B.Cu at (147.6, 109.8)
- added H3: MountingHole_Pad, Kicad_Library:ThroughHoleSingleSide_1mm_1.6mm, B.Cu at (160.3, 51.3)
- added H3: MountingHole_Pad, Kicad_Library:ThroughHoleSingleSide_1mm_1.6mm, B.Cu at (162.9, 51.3)
- added H3: MountingHole_Pad, Kicad_Library:ThroughHoleSingleSide_1mm_1.6mm, B.Cu at (165.4, 51.3)
- added H3: MountingHole_Pad, Kicad_Library:ThroughHoleSingleSide_1mm_1.6mm, B.Cu at (167.9, 51.3)
- added H3: MountingHole_Pad, Kicad_Library:ThroughHoleSingleSide_1mm_1.6mm, B.Cu at (170.5, 51.3)
- added H3: MountingHole_Pad, Kicad_Library:ThroughHoleSingleSide_1mm_1.6mm, B.Cu at (173.0, 51.3)
- added H3: MountingHole_Pad, Kicad_Library:ThroughHoleSingleSide_1mm_1.6mm, B.Cu at (175.6, 51.3)
- added H3: MountingHole_Pad, Kicad_Library:ThroughHoleSingleSide_1mm_1.6mm, B.Cu at (178.1, 51.3)
- added H3: MountingHole_Pad, Kicad_Library:ThroughHoleSingleSide_1mm_1.6mm, B.Cu at (180.7, 51.3)
- added H3: MountingHole_Pad, Kicad_Library:ThroughHoleSingleSide_1mm_1.6mm, B.Cu at (183.2, 51.3)
- added H3: MountingHole_Pad, Kicad_Library:ThroughHoleSingleSide_1mm_1.6mm, B.Cu at (150.2, 109.8)
- added H3: MountingHole_Pad, Kicad_Library:ThroughHoleSingleSide_1mm_1.6mm, B.Cu at (185.7, 51.3)
- added H3: MountingHole_Pad, Kicad_Library:ThroughHoleSingleSide_1mm_1.6mm, B.Cu at (188.3, 51.3)
- added H3: MountingHole_Pad, Kicad_Library:ThroughHoleSingleSide_1mm_1.6mm, B.Cu at (190.8, 51.3)
- added H3: MountingHole_Pad, Kicad_Library:ThroughHoleSingleSide_1mm_1.6mm, B.Cu at (193.3, 51.3)
- added H3: MountingHole_Pad, Kicad_Library:ThroughHoleSingleSide_1mm_1.6mm, B.Cu at (195.9, 51.3)
- added H3: MountingHole_Pad, Kicad_Library:ThroughHoleSingleSide_1mm_1.6mm, B.Cu at (198.4, 51.3)
- added H3: MountingHole_Pad, Kicad_Library:ThroughHoleSingleSide_1mm_1.6mm, B.Cu at (201.0, 51.3)
- added H3: MountingHole_Pad, Kicad_Library:ThroughHoleSingleSide_1mm_1.6mm, B.Cu at (203.5, 51.3)
- added H3: MountingHole_Pad, Kicad_Library:ThroughHoleSingleSide_1mm_1.6mm, B.Cu at (206.1, 51.3)
- added H3: MountingHole_Pad, Kicad_Library:ThroughHoleSingleSide_1mm_1.6mm, B.Cu at (208.6, 51.3)
- added H3: MountingHole_Pad, Kicad_Library:ThroughHoleSingleSide_1mm_1.6mm, B.Cu at (152.7, 109.8)
- added H3: MountingHole_Pad, Kicad_Library:ThroughHoleSingleSide_1mm_1.6mm, B.Cu at (211.1, 51.3)
- added H3: MountingHole_Pad, Kicad_Library:ThroughHoleSingleSide_1mm_1.6mm, B.Cu at (213.7, 51.3)
- added H3: MountingHole_Pad, Kicad_Library:ThroughHoleSingleSide_1mm_1.6mm, B.Cu at (216.2, 51.3)
- added H3: MountingHole_Pad, Kicad_Library:ThroughHoleSingleSide_1mm_1.6mm, B.Cu at (218.8, 51.3)
- added H3: MountingHole_Pad, Kicad_Library:ThroughHoleSingleSide_1mm_1.6mm, B.Cu at (221.3, 51.3)
- added H3: MountingHole_Pad, Kicad_Library:ThroughHoleSingleSide_1mm_1.6mm, B.Cu at (223.8, 51.3)
- added H3: MountingHole_Pad, Kicad_Library:ThroughHoleSingleSide_1mm_1.6mm, B.Cu at (107.0, 48.8)
- added H3: MountingHole_Pad, Kicad_Library:ThroughHoleSingleSide_1mm_1.6mm, B.Cu at (109.5, 48.8)
- added H3: MountingHole_Pad, Kicad_Library:ThroughHoleSingleSide_1mm_1.6mm, B.Cu at (112.1, 48.8)
- added H3: MountingHole_Pad, Kicad_Library:ThroughHoleSingleSide_1mm_1.6mm, B.Cu at (114.6, 48.8)
- added H3: MountingHole_Pad, Kicad_Library:ThroughHoleSingleSide_1mm_1.6mm, B.Cu at (155.2, 109.8)
- added H3: MountingHole_Pad, Kicad_Library:ThroughHoleSingleSide_1mm_1.6mm, B.Cu at (117.2, 48.8)
- added H3: MountingHole_Pad, Kicad_Library:ThroughHoleSingleSide_1mm_1.6mm, B.Cu at (119.7, 48.8)
- added H3: MountingHole_Pad, Kicad_Library:ThroughHoleSingleSide_1mm_1.6mm, B.Cu at (122.2, 48.8)
- added H3: MountingHole_Pad, Kicad_Library:ThroughHoleSingleSide_1mm_1.6mm, B.Cu at (124.8, 48.8)
- added H3: MountingHole_Pad, Kicad_Library:ThroughHoleSingleSide_1mm_1.6mm, B.Cu at (127.3, 48.8)
- added H3: MountingHole_Pad, Kicad_Library:ThroughHoleSingleSide_1mm_1.6mm, B.Cu at (129.8, 48.8)
- added H3: MountingHole_Pad, Kicad_Library:ThroughHoleSingleSide_1mm_1.6mm, B.Cu at (132.4, 48.8)
- added H3: MountingHole_Pad, Kicad_Library:ThroughHoleSingleSide_1mm_1.6mm, B.Cu at (134.9, 48.8)
- added H3: MountingHole_Pad, Kicad_Library:ThroughHoleSingleSide_1mm_1.6mm, B.Cu at (137.5, 48.8)
- added H3: MountingHole_Pad, Kicad_Library:ThroughHoleSingleSide_1mm_1.6mm, B.Cu at (140.0, 48.8)
- added H3: MountingHole_Pad, Kicad_Library:ThroughHoleSingleSide_1mm_1.6mm, B.Cu at (122.2, 114.8)
- added H3: MountingHole_Pad, Kicad_Library:ThroughHoleSingleSide_1mm_1.6mm, B.Cu at (157.8, 109.8)
- added H3: MountingHole_Pad, Kicad_Library:ThroughHoleSingleSide_1mm_1.6mm, B.Cu at (142.6, 48.8)
- added H3: MountingHole_Pad, Kicad_Library:ThroughHoleSingleSide_1mm_1.6mm, B.Cu at (145.1, 48.8)
- added H3: MountingHole_Pad, Kicad_Library:ThroughHoleSingleSide_1mm_1.6mm, B.Cu at (147.6, 48.8)
- added H3: MountingHole_Pad, Kicad_Library:ThroughHoleSingleSide_1mm_1.6mm, B.Cu at (150.2, 48.8)
- added H3: MountingHole_Pad, Kicad_Library:ThroughHoleSingleSide_1mm_1.6mm, B.Cu at (152.7, 48.8)
- added H3: MountingHole_Pad, Kicad_Library:ThroughHoleSingleSide_1mm_1.6mm, B.Cu at (155.2, 48.8)
- added H3: MountingHole_Pad, Kicad_Library:ThroughHoleSingleSide_1mm_1.6mm, B.Cu at (157.8, 48.8)
- added H3: MountingHole_Pad, Kicad_Library:ThroughHoleSingleSide_1mm_1.6mm, B.Cu at (160.3, 48.8)
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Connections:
- U1 pad a1: (no net) -> /SPARE_B
- U1 pad a2: (no net) -> /EN_JTAG_B
- U1 pad a3: (no net) -> /EN_ICSP_B
- U1 pad a4: (no net) -> /EN_PWR_B
- U1 pad c1: (no net) -> /SPARE_A
- U1 pad c10: (no net) -> /TCK
- U1 pad c11: (no net) -> /TMS
- U1 pad c12: (no net) -> /TDO
- U1 pad c13: (no net) -> /TDI
- U1 pad c2: (no net) -> /EN_JTAG_A
- U1 pad c3: (no net) -> /EN_ICSP_A
- U1 pad c4: (no net) -> /EN_PWR_A
- U1 pad c5: (no net) -> /TARGET_TX
- U1 pad c6: (no net) -> /TARGET_RX
- U1 pad c7: (no net) -> /PGED
- U1 pad c8: (no net) -> /PGEC
- U1 pad c9: (no net) -> /~MCLR
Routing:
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- added copper zone on B.Cu, net GND
- added copper zone on F.Cu, net GND
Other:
- board size 150 x 76 mm -> 185 x 76 mm
- board text added: "A"
- board text added: "B"

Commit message: Mid-work commit. IT's not pretty but it'll work
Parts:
- moved RN2 52.1 mm to (50.0, 52.9)
- moved RN1 48.1 mm to (50.0, 101.1)
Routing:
- net +3V3: track 19.6 -> 337.6 mm, vias 0 -> 7
- net GND: track 3.34 -> 319.3 mm, vias 14 -> 48
- net /EN_ICSP_B: track 0.00 -> 262.5 mm, vias 0 -> 2
- net /EN_ICSP_A: track 0.00 -> 253.0 mm, vias 0 -> 11
- net /EN_JTAG_A: track 0.00 -> 247.5 mm, vias 0 -> 10
- net /EN_JTAG_B: track 0.00 -> 223.5 mm, vias 0 -> 2
- net VDD: track 0.00 -> 133.5 mm, vias 0 -> 8
- net /~MCLR: track 29.8 -> 77.4 mm, vias 2 -> 4
- net /EN_PWR_A: track 14.5 -> 62.1 mm
- net /EN_PWR_B: track 15.8 -> 62.7 mm, vias 0 -> 2
- net /TARGET_RX: track 32.9 -> 74.7 mm, vias 2 -> 6
- net /TARGET_TX: track 29.8 -> 70.4 mm, vias 0 -> 4
- net /TDI: track 9.45 -> 50.1 mm, vias 0 -> 2
- net /A_~MCLR: track 30.0 -> 70.2 mm, vias 2 -> 4
- net /TDO: track 8.93 -> 47.5 mm, vias 0 -> 2
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
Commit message: Mid-work commit. Added notes, figured out what works, etc.
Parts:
- moved J5 0.50 mm to (215.5, 58.2)
- moved RN2 0.30 mm to (50.0, 53.2)
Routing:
- net /UNUSED_B_1: track 0.00 -> 46.0 mm, vias 0 -> 4
- net /UNUSED_B_2: track 0.00 -> 45.9 mm, vias 0 -> 4
- net +3V3: track 337.6 -> 357.8 mm, vias 7 -> 10
- net /EN_ICSP_A: track 253.0 -> 254.4 mm
- net /B_TDI: track 47.5 -> 48.3 mm
- net /B_TDO: track 42.4 -> 43.1 mm
- net GND: vias 48 -> 169
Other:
- board text added: "GND"
- board text added: "ICSP A"
- board text added: "ICSP B"
- board text added: "JTAG A"
- board text added: "JTAG B"
- board text added: "PGEC"
- board text added: "PGED"
- board text added: "RX"
- board text added: "SPARE"
- board text added: "TCK"
- board text added: "TDI"
- board text added: "TDO"
- board text added: "TMS"
- board text added: "TX"
- board text added: "VCC"
- board text added: "VDD"
- board text added: "~MCLR~"
